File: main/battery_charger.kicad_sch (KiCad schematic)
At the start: 46 parts, among them Q1601 IXTP28P065T, Q1603 Q_NMOS_DGS, Q1604 IXTP28P065T, Q1605 TK4R3E06PL, Q1606 Q_NMOS_GDS, Q1608 IXTP28P065T, U1601 LT8710, U1701 TMCS1101A3x-Q1, U1702 LM321

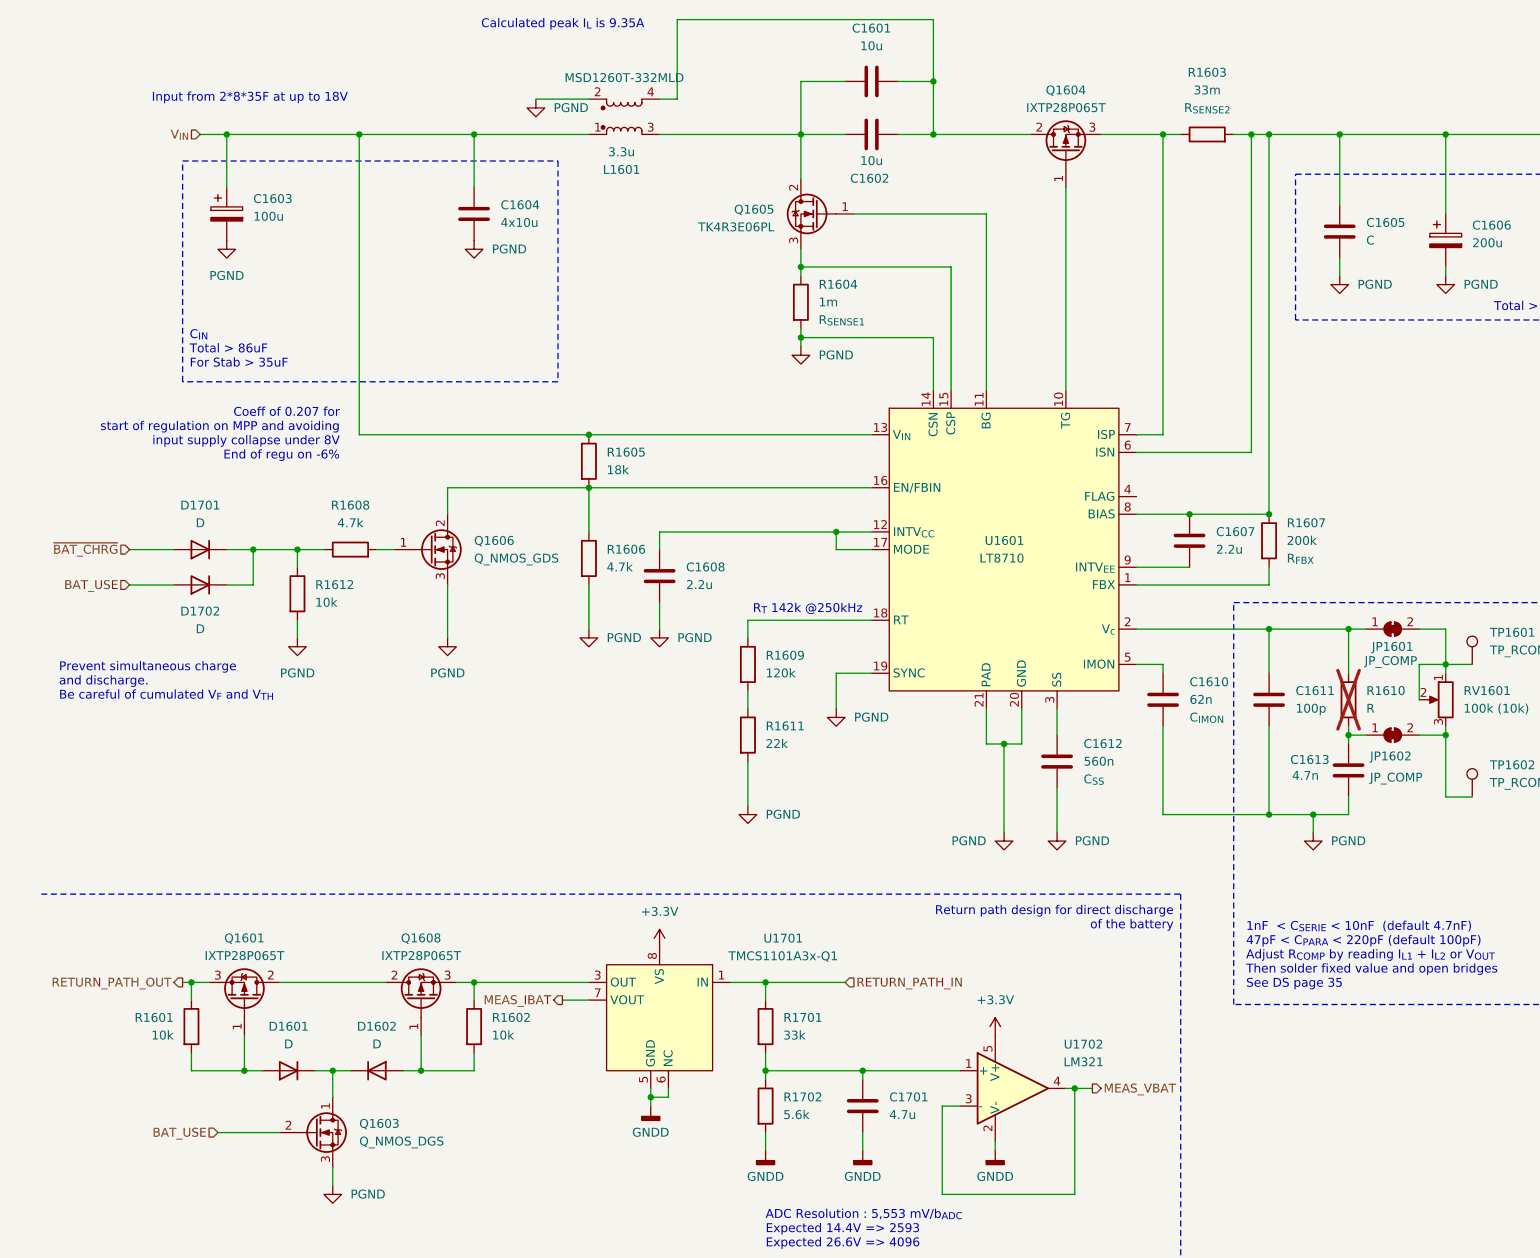
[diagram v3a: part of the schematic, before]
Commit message: Finalize sch and start component mapping
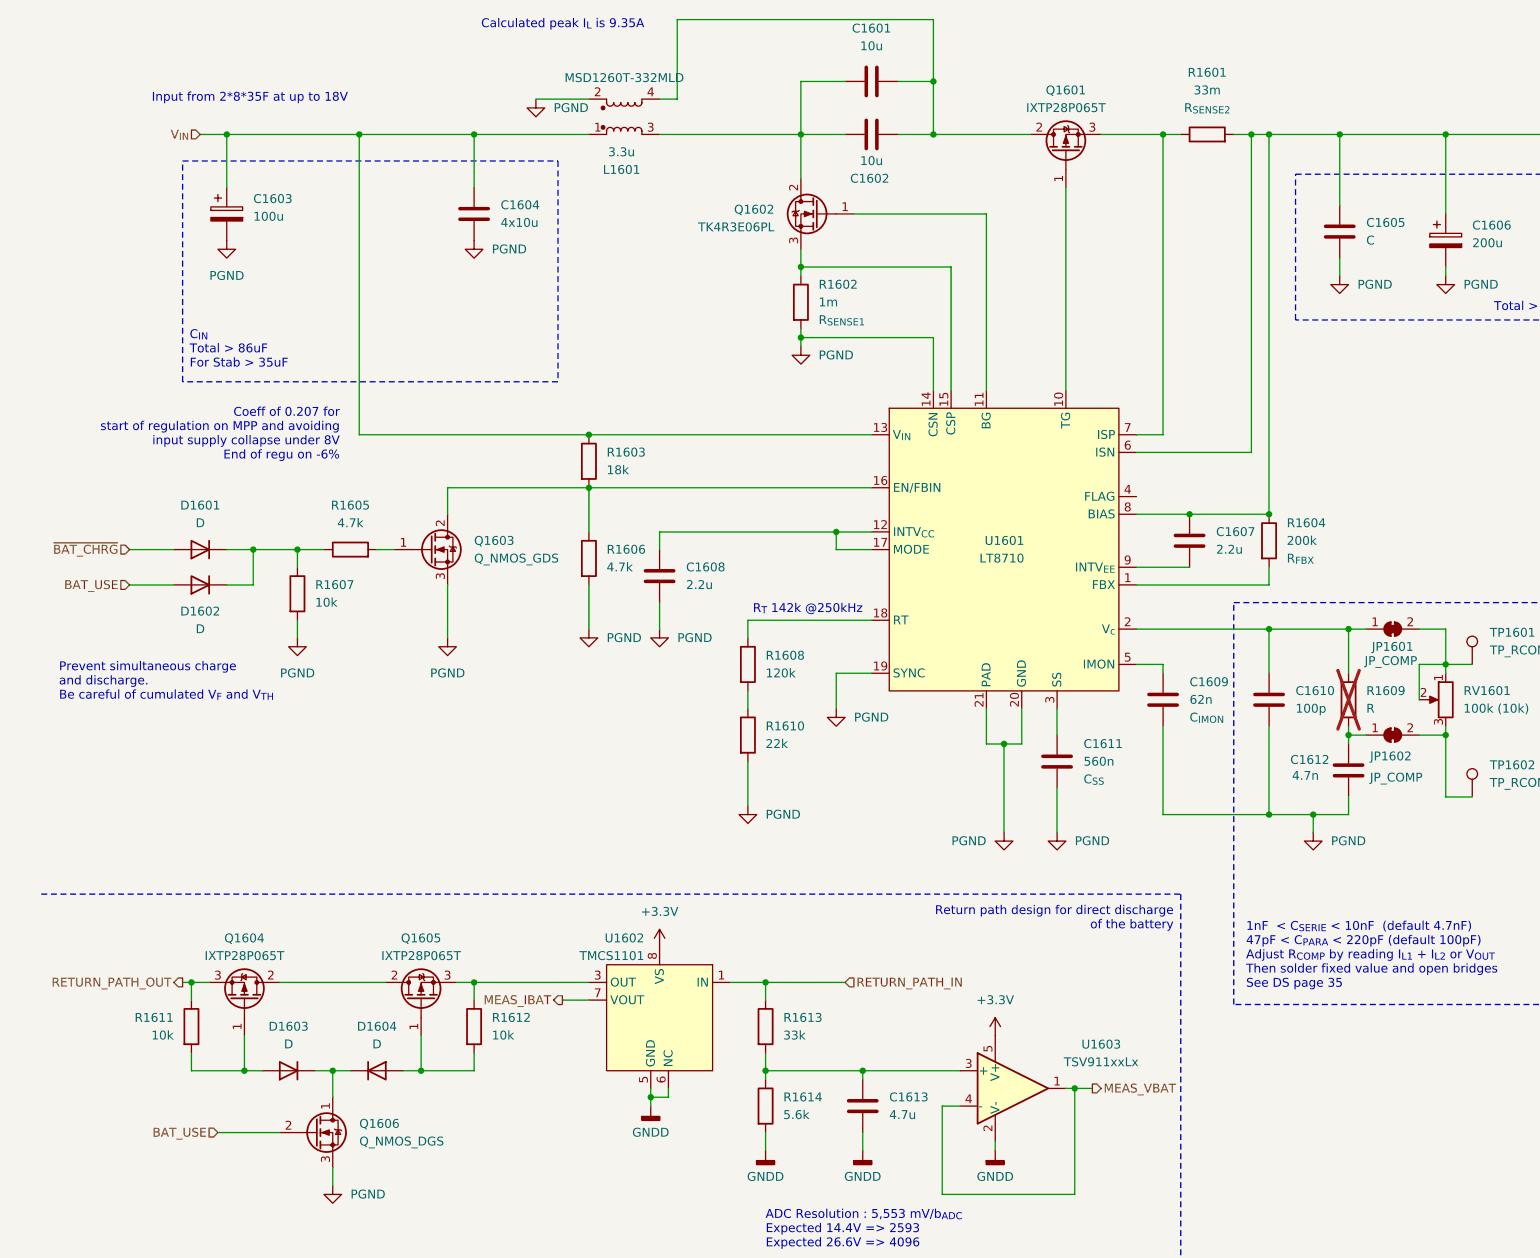
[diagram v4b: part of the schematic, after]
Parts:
- removed U1701: TMCS1101A3x-Q1, symbol dsv4:TMCS1101
- added U1602: TMCS1101, symbol dsv4:TMCS1101
- C1601, C1602, C1607, C1608: footprint (none) -> Capacitor_SMD:C_0805_2012Metric
- C1609: renamed from C1610; footprint (none) -> Capacitor_SMD:C_0805_2012Metric
- C1610: renamed from C1611; footprint (none) -> Capacitor_SMD:C_0805_2012Metric
- C1611: renamed from C1612; footprint (none) -> Capacitor_SMD:C_0805_2012Metric
- C1612: renamed from C1613; footprint (none) -> Capacitor_SMD:C_0805_2012Metric
- C1613: renamed from C1701; footprint (none) -> Capacitor_SMD:C_0805_2012Metric; now in the parts list
- JP1601, JP1602: footprint (none) -> Jumper:SolderJumper-2_P1.3mm_Open_TrianglePad1.0x1.5mm
- Q1601: renamed from Q1604; footprint (none) -> Package_TO_SOT_THT:TO-220-3_Horizontal_TabUp
- Q1604: renamed from Q1601; footprint (none) -> Package_TO_SOT_THT:TO-220-3_Horizontal_TabUp
- Q1605: renamed from Q1608; footprint (none) -> Package_TO_SOT_THT:TO-220-3_Horizontal_TabUp
- R1603: renamed from R1605; footprint (none) -> Resistor_SMD:R_0805_2012Metric
- R1604: renamed from R1607; footprint (none) -> Resistor_SMD:R_0805_2012Metric
- R1605: renamed from R1608; footprint (none) -> Resistor_SMD:R_0805_2012Metric
- R1606: footprint (none) -> Resistor_SMD:R_0805_2012Metric
- R1607: renamed from R1612; footprint (none) -> Resistor_SMD:R_0805_2012Metric
- R1608: renamed from R1609; footprint (none) -> Resistor_SMD:R_0805_2012Metric
- R1609: renamed from R1610; footprint (none) -> Resistor_SMD:R_0805_2012Metric
- R1610: renamed from R1611; footprint (none) -> Resistor_SMD:R_0805_2012Metric
- R1611: renamed from R1601; footprint (none) -> Resistor_SMD:R_0805_2012Metric
- R1612: renamed from R1602; footprint (none) -> Resistor_SMD:R_0805_2012Metric; now in the parts list
- R1613: renamed from R1701; footprint (none) -> Resistor_SMD:R_0805_2012Metric; now in the parts list
- R1614: renamed from R1702; footprint (none) -> Resistor_SMD:R_0805_2012Metric; now in the parts list
- U1603: renamed from U1702; value LM321 -> TSV911xxLx; symbol Amplifier_Operational:LM321 -> Amplifier_Operational:TSV911xxLx; now in the parts list
- renumbered D1701 to D1601, D1702 to D1602, D1601 to D1603, D1602 to D1604, Q1605 to Q1602, Q1606 to Q1603, Q1603 to Q1606, R1603 to R1601, R1604 to R1602
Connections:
- net +3.3V: now also U1602.8 (VS)
- net GNDD: now also U1602.5 (GND), U1602.6 (NC)
- net IN: now also U1602.1 (IN), U1602.2 (IN)
- net MEAS_IBAT: now also U1602.7 (VOUT)
- net MEAS_VBAT: now also U1603.1; no longer U1603.3 (-)
- net at C1613.1, R1613.2, R1614.1: now also U1603.3 (+); no longer U1603.1 (+)
- net at Q1605.3 (S), R1612.1: now also U1602.3 (OUT), U1602.4 (OUT)

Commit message: update BOM
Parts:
- removed C1603: 100u, symbol Device:C_Polarized
- added C1603, C1614, C1615: 10u, Capacitor_SMD:C_0805_2012Metric, symbol Device:C
- C1604: value 4x10u -> 10u; footprint (none) -> Capacitor_SMD:C_0805_2012Metric
- TP1601, TP1602: footprint (none) -> TestPoint:TestPoint_Keystone_5010-5014_Multipurpose
- U1602: footprint (none) -> Package_SO:SOIC-8_3.9x4.9mm_P1.27mm
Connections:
- net PGND: now also C1603.2, C1614.2, C1615.2
- net V_{IN}: now also C1614.1, C1615.1; no longer C1604.1

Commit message: BOM OK
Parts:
- removed C1605: C, symbol Device:C
- removed D1601, D1602, D1603, D1604: D, symbol Device:D
- removed Q1603: Q_NMOS_GDS, symbol Device:Q_NMOS_GDS
- removed Q1606: Q_NMOS_DGS, symbol Device:Q_NMOS_DGS
- added C1605: 100u, Capacitor_THT:CP_Radial_D6.3mm_P2.50mm, symbol Device:C_Polarized
- added D1601, D1602, D1603, D1604: B5819W-TP, Diode_SMD:D_SOD-123, symbol Device:D_Schottky
- added Q1603, Q1606: IRLML0030, Package_TO_SOT_SMD:SOT-23, symbol Transistor_FET:IRLML0030
- C1606: value 200u -> 100u; footprint (none) -> Capacitor_THT:CP_Radial_D6.3mm_P2.50mm
- L1601: footprint (none) -> dsv4:Coilcraft_MSD1260T
- R1601: footprint (none) -> Resistor_SMD:R_2010_5025Metric; MPN (none) -> TLM2HDR033FTE
- R1602: footprint (none) -> Resistor_SMD:R_2010_5025Metric
- RV1601: footprint (none) -> Potentiometer_THT:Potentiometer_Bourns_3296W_Vertical
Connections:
- net BAT_USE: now also D1602.2 (A), Q1606.1 (G)
- net PGND: now also C1605.2, Q1603.2 (S), Q1606.2 (S)
- net V_{OUT}: now also C1605.1
- net ~{BAT_CHRG}: now also D1601.2 (A)
- net at R1603.2, R1606.1, U1601.16 (EN/FBIN): now also Q1603.3 (D)
- net at R1605.2: now also Q1603.1 (G)
- net at Q1605.1 (G), R1612.2: now also D1604.2 (A)
- net at R1605.1, R1607.1: now also D1601.1 (K), D1602.1 (K)
- net at Q1604.1 (G), R1611.2: now also D1603.2 (A)
- new net: D1603.1 (K), D1604.1 (K), Q1606.3 (D)

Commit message: Update PCB
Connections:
- net PGND: now also L1601.1; no longer L1601.2
- net V_{IN}: now also C1603.1, C1604.1, L1601.2; no longer L1601.1
- net SW_IN: now reaches C1601.2, C1602.2, Q1602.2 (D)
- net SW_IN: now also L1601.4; no longer L1601.3
- net SWIN_CSP: now reaches Q1602.3 (S), R1602.1, U1601.15 (CSP)
- net SW_OUT: now reaches C1601.1, C1602.1, Q1601.2 (D)
- net SW_OUT: now also L1601.3; no longer L1601.4
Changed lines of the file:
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@@
 	)
 	(junction
+		(at 49.53 34.29)
+		(diameter 0)
+		(color 0 0 0 0)
+	)
+	(junction
 		(at 73.66 34.29)
 		(diameter 0)
@@
 	)
 	(junction
+		(at 60.96 34.29)
+		(diameter 0)
+		(color 0 0 0 0)
+	)
+	(junction
 		(at 187.96 88.9)
 		(diameter 0)
@@
 	(wire
 		(pts
+			(xy 60.96 34.29) (xy 73.66 34.29)
+		)
+		(stroke
+			(width 0)
+			(type default)
+		)
+	)
+	(wire
+		(pts
 			(xy 129.54 168.91) (xy 143.51 168.91)
 		)
@@
 	(wire
 		(pts
-			(xy 38.1 34.29) (xy 73.66 34.29)
+			(xy 38.1 34.29) (xy 49.53 34.29)
 		)
 		(stroke
@@
 	(wire
 		(pts
+			(xy 49.53 34.29) (xy 49.53 41.91)
+		)
+		(stroke
+			(width 0)
+			(type default)
+		)
+	)
+	(wire
+		(pts
 			(xy 40.64 168.91) (xy 43.18 168.91)
 		)
@@
 	(wire
 		(pts
+			(xy 49.53 34.29) (xy 60.96 34.29)
+		)
+		(stroke
+			(width 0)
+			(type default)
+		)
+	)
+	(wire
+		(pts
 			(xy 152.4 121.92) (xy 152.4 116.84)
 		)
@@
 	(wire
 		(pts
+			(xy 60.96 34.29) (xy 60.96 41.91)
+		)
+		(stroke
+			(width 0)
+			(type default)
+		)
+	)
+	(wire
+		(pts
 			(xy 160.02 171.45) (xy 162.56 171.45)
 		)
@@
 		)
 	)
+	(label "SW_OUT"
+		(at 109.22 17.78 0)
+		(fields_autoplaced yes)
+		(effects
+			(font
+				(size 1.27 1.27)
+			)
+			(justify left bottom)
+		)
+	)
+	(label "SWIN_CSP"
+		(at 125.7121 53.34 0)
+		(fields_autoplaced yes)
+		(effects
+			(font
+				(size 1.27 1.27)
+			)
+			(justify left bottom)
+		)
+	)
+	(label "SW_IN"
+		(at 109.22 34.29 0)
+		(fields_autoplaced yes)
+		(effects
+			(font
+				(size 1.27 1.27)
+			)
+			(justify left bottom)
+		)
+	)
 	(hierarchical_label "MEAS_VBAT"
 		(shape output)
@@
 		(lib_id "Device:L_Coupled_1324")
 		(at 95.25 31.75 0)
-		(mirror x)
 		(unit 1)
 		(exclude_from_sim no)
@@
 		(dnp no)
 		(property "Reference" "L1601"
-			(at 94.869 39.37 0)
+			(at 94.869 24.13 0)
 			(effects
 				(font
@@
 		)
 		(property "Value" "3.3u"
-			(at 94.869 36.83 0)
+			(at 94.869 26.67 0)
 			(effects
 				(font
@@
 		)
 		(property "MPN" " MSD1260T-332MLD "
-			(at 95.25 26.162 0)
+			(at 95.25 37.338 0)
 			(effects
 				(font
